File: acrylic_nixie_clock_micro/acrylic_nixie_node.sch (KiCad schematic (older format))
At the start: 10 parts

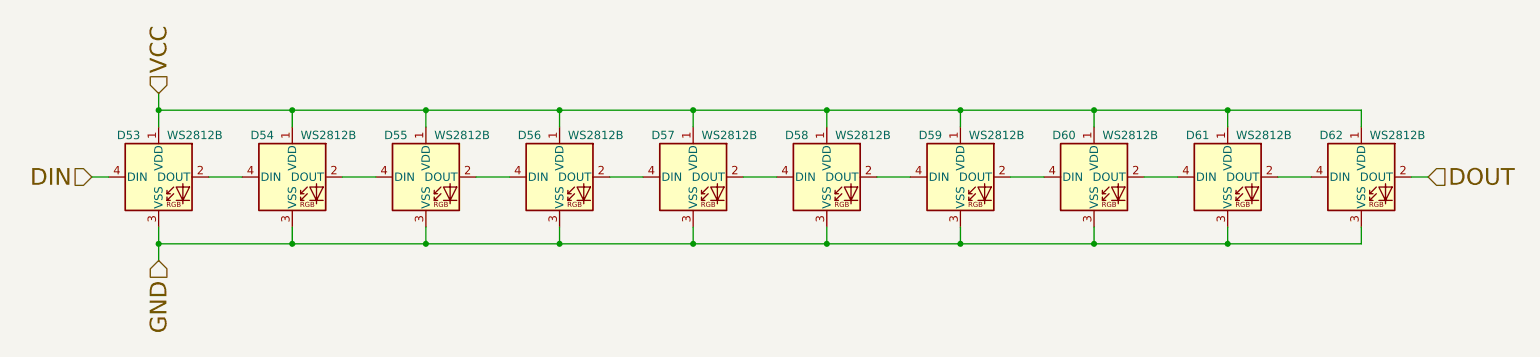
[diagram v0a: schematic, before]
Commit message: 問題点を修正
CH304Gの電源電圧を3.3Vに
RSTにコンデンサを追加
USBのフットプリントを修正
カードコネクタの追加
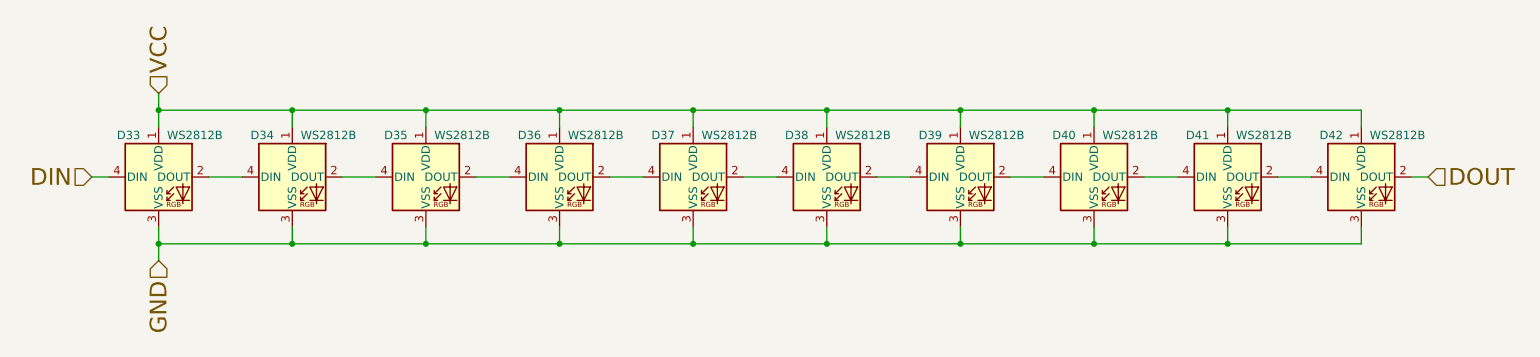
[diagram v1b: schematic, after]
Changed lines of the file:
@@
 $Descr A4 11693 8268
 encoding utf-8
-Sheet 5 10
+Sheet 6 10
 Title ""
 Date ""
@@
 AR Path="/5F60D2EB/5F5DDD85/5F5D7969" Ref="D13"  Part="1"
 AR Path="/5F60D2EB/5F5DE4EE/5F5D7969" Ref="D3"  Part="1"
-F 0 "D53" H 1750 2800 50  0000 L CNN
+F 0 "D33" H 1750 2800 50  0000 L CNN
 F 1 "WS2812B" H 2050 2800 50  0000 L CNN
 F 2 "LED_SMD:LED_WS2812B_PLCC4_5.0x5.0mm_P3.2mm" H 2050 2250 50  0001 L TNN
@@
 AR Path="/5F60D2EB/5F5DDD85/5F5DEB9F" Ref="D14"  Part="1"
 AR Path="/5F60D2EB/5F5DE4EE/5F5DEB9F" Ref="D4"  Part="1"
-F 0 "D54" H 2550 2800 50  0000 L CNN
+F 0 "D34" H 2550 2800 50  0000 L CNN
 F 1 "WS2812B" H 2850 2800 50  0000 L CNN
 F 2 "LED_SMD:LED_WS2812B_PLCC4_5.0x5.0mm_P3.2mm" H 2850 2250 50  0001 L TNN
@@
 AR Path="/5F60D2EB/5F5DDD85/5F5E1DA0" Ref="D15"  Part="1"
 AR Path="/5F60D2EB/5F5DE4EE/5F5E1DA0" Ref="D5"  Part="1"
-F 0 "D55" H 3350 2800 50  0000 L CNN
+F 0 "D35" H 3350 2800 50  0000 L CNN
 F 1 "WS2812B" H 3650 2800 50  0000 L CNN
 F 2 "LED_SMD:LED_WS2812B_PLCC4_5.0x5.0mm_P3.2mm" H 3650 2250 50  0001 L TNN
@@
 AR Path="/5F60D2EB/5F5DDD85/5F5E1DA7" Ref="D16"  Part="1"
 AR Path="/5F60D2EB/5F5DE4EE/5F5E1DA7" Ref="D6"  Part="1"
-F 0 "D56" H 4150 2800 50  0000 L CNN
+F 0 "D36" H 4150 2800 50  0000 L CNN
 F 1 "WS2812B" H 4450 2800 50  0000 L CNN
 F 2 "LED_SMD:LED_WS2812B_PLCC4_5.0x5.0mm_P3.2mm" H 4450 2250 50  0001 L TNN
@@
 AR Path="/5F60D2EB/5F5DDD85/5F5E3D0E" Ref="D17"  Part="1"
 AR Path="/5F60D2EB/5F5DE4EE/5F5E3D0E" Ref="D7"  Part="1"
-F 0 "D57" H 4950 2800 50  0000 L CNN
+F 0 "D37" H 4950 2800 50  0000 L CNN
 F 1 "WS2812B" H 5250 2800 50  0000 L CNN
 F 2 "LED_SMD:LED_WS2812B_PLCC4_5.0x5.0mm_P3.2mm" H 5250 2250 50  0001 L TNN
@@
 AR Path="/5F60D2EB/5F5DDD85/5F5E3D15" Ref="D18"  Part="1"
 AR Path="/5F60D2EB/5F5DE4EE/5F5E3D15" Ref="D8"  Part="1"
-F 0 "D58" H 5750 2800 50  0000 L CNN
+F 0 "D38" H 5750 2800 50  0000 L CNN
 F 1 "WS2812B" H 6050 2800 50  0000 L CNN
 F 2 "LED_SMD:LED_WS2812B_PLCC4_5.0x5.0mm_P3.2mm" H 6050 2250 50  0001 L TNN
@@
 AR Path="/5F60D2EB/5F5DDD85/5F5E8AFC" Ref="D19"  Part="1"
 AR Path="/5F60D2EB/5F5DE4EE/5F5E8AFC" Ref="D9"  Part="1"
-F 0 "D59" H 6550 2800 50  0000 L CNN
+F 0 "D39" H 6550 2800 50  0000 L CNN
 F 1 "WS2812B" H 6850 2800 50  0000 L CNN
 F 2 "LED_SMD:LED_WS2812B_PLCC4_5.0x5.0mm_P3.2mm" H 6850 2250 50  0001 L TNN
@@
 AR Path="/5F60D2EB/5F5DDD85/5F5E8B03" Ref="D20"  Part="1"
 AR Path="/5F60D2EB/5F5DE4EE/5F5E8B03" Ref="D10"  Part="1"
-F 0 "D60" H 7350 2800 50  0000 L CNN
+F 0 "D40" H 7350 2800 50  0000 L CNN
 F 1 "WS2812B" H 7650 2800 50  0000 L CNN
 F 2 "LED_SMD:LED_WS2812B_PLCC4_5.0x5.0mm_P3.2mm" H 7650 2250 50  0001 L TNN
@@
 AR Path="/5F60D2EB/5F5DDD85/5F5EAE84" Ref="D21"  Part="1"
 AR Path="/5F60D2EB/5F5DE4EE/5F5EAE84" Ref="D11"  Part="1"
-F 0 "D61" H 8150 2800 50  0000 L CNN
+F 0 "D41" H 8150 2800 50  0000 L CNN
 F 1 "WS2812B" H 8450 2800 50  0000 L CNN
 F 2 "LED_SMD:LED_WS2812B_PLCC4_5.0x5.0mm_P3.2mm" H 8450 2250 50  0001 L TNN
@@
 AR Path="/5F60D2EB/5F5DDD85/5F5EAE8B" Ref="D22"  Part="1"
 AR Path="/5F60D2EB/5F5DE4EE/5F5EAE8B" Ref="D12"  Part="1"
-F 0 "D62" H 8950 2800 50  0000 L CNN
+F 0 "D42" H 8950 2800 50  0000 L CNN
 F 1 "WS2812B" H 9250 2800 50  0000 L CNN
 F 2 "LED_SMD:LED_WS2812B_PLCC4_5.0x5.0mm_P3.2mm" H 9250 2250 50  0001 L TNN
